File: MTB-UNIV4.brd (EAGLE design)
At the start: 100 x 80 mm, 91 parts, among them IC1 MEGA128-A, IC2 SN75176AP, IC3 NCP1117, IC4 ULN2803A, IC5 ULN2803A, X1 MKDSN1,5/4-5,08, X2 MKDSN1,5/4-5,08

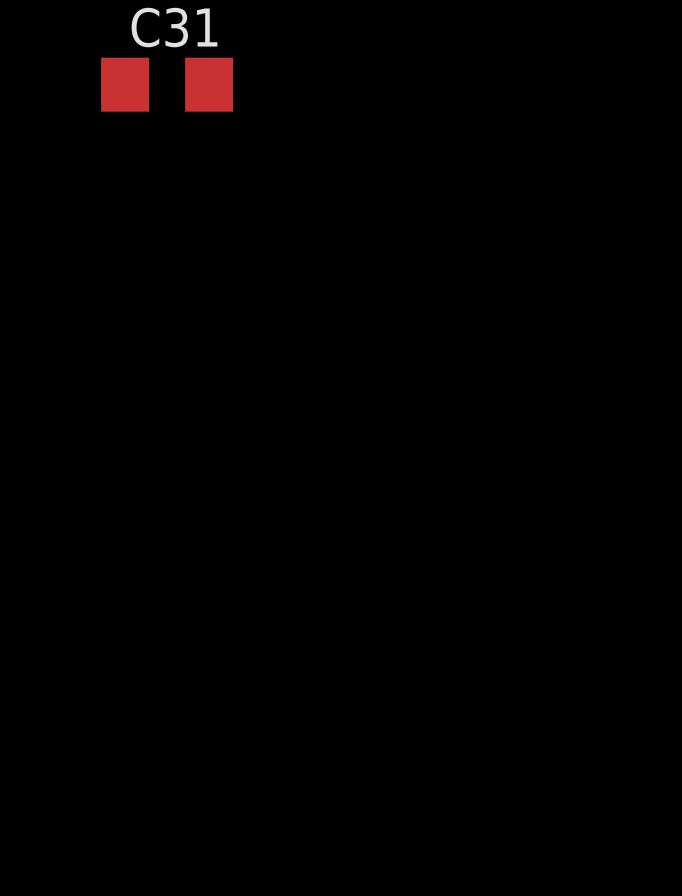
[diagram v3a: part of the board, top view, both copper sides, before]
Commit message: To stejné jako na vstupech ULN jsem udělal i na vstupu stabilizátoru. Tyristor v Crowbar obvodu proti přepětí.
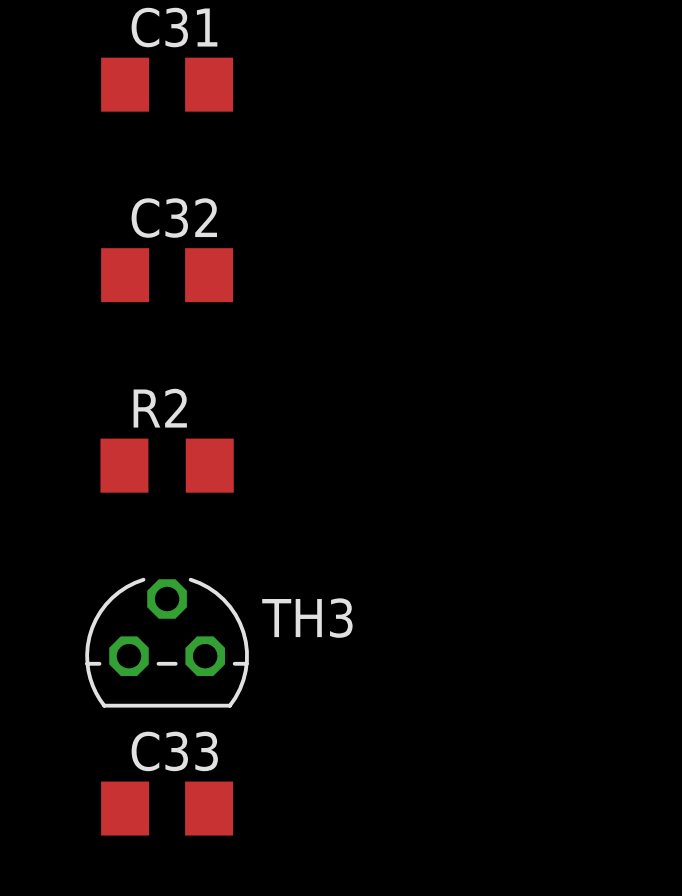
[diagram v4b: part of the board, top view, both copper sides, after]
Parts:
- added C32, C33: 100nF, rcl:C1206
- added R2: 2k2, rcl:R1206
- added TH3: MCR100, ElectroKrt:TO92
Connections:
- removed net N$14: D1.A, D2.C, F1.2
- new net N$57: C33.1, D2.A, R2.2, TH3.2
- new net N$58: C32.1, D1.A, F1.2
- net GND: now also C32.2, C33.2, R2.1, TH3.1; no longer D2.A
- net N$13: now also D2.C, TH3.3
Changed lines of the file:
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@@
 <attribute name="VALUE" x="-74.93" y="-614.68" size="1.27" layer="27"/>
+</element>
+<element name="C32" library="rcl" library_urn="urn:adsk.eagle:library:334" package="C1206" package3d_urn="urn:adsk.eagle:package:23618/2" value="100nF" x="-73.66" y="-618.49" smashed="yes">
+<attribute name="NAME" x="-74.93" y="-617.22" size="1.27" layer="25"/>
+<attribute name="POPULARITY" value="54" x="-73.66" y="-618.49" size="1.778" layer="27" display="off"/>
+<attribute name="SPICEPREFIX" value="C" x="-73.66" y="-618.49" size="1.778" layer="27" display="off"/>
+<attribute name="VALUE" x="-74.93" y="-621.03" size="1.27" layer="27"/>
+</element>
+<element name="R2" library="rcl" library_urn="urn:adsk.eagle:library:334" package="R1206" package3d_urn="urn:adsk.eagle:package:23540/2" value="2k2" x="-73.66" y="-624.84" smashed="yes">
+<attribute name="NAME" x="-74.93" y="-623.57" size="1.27" layer="25"/>
+<attribute name="POPULARITY" value="41" x="-73.66" y="-624.84" size="1.778" layer="27" display="off"/>
+<attribute name="SPICEPREFIX" value="R" x="-73.66" y="-624.84" size="1.778" layer="27" display="off"/>
+<attribute name="VALUE" x="-74.93" y="-627.38" size="1.27" layer="27"/>
+</element>
+<element name="TH3" library="ElectroKrt" package="TO92" package3d_urn="urn:adsk.eagle:package:28523/2" value="MCR100" x="-73.66" y="-631.19" smashed="yes">
+<attribute name="NAME" x="-70.485" y="-630.555" size="1.27" layer="25" ratio="10"/>
+<attribute name="PACKAGE" value="TO-92" x="-73.66" y="-631.19" size="1.778" layer="27" display="off"/>
+<attribute name="VALUE" x="-70.485" y="-632.46" size="1.27" layer="27" ratio="10"/>
+</element>
+<element name="C33" library="rcl" library_urn="urn:adsk.eagle:library:334" package="C1206" package3d_urn="urn:adsk.eagle:package:23618/2" value="100nF" x="-73.66" y="-636.27" smashed="yes">
+<attribute name="NAME" x="-74.93" y="-635" size="1.27" layer="25"/>
+<attribute name="POPULARITY" value="54" x="-73.66" y="-636.27" size="1.778" layer="27" display="off"/>
+<attribute name="SPICEPREFIX" value="C" x="-73.66" y="-636.27" size="1.778" layer="27" display="off"/>
+<attribute name="VALUE" x="-74.93" y="-638.81" size="1.27" layer="27"/>
 </element>
 </elements>
@@
 <contactref element="C8" pad="2"/>
 <contactref element="IC3" pad="1"/>
-<contactref element="D2" pad="A"/>
 <contactref element="C3" pad="2"/>
 <contactref element="X1" pad="4"/>
@@
 <contactref element="C31" pad="2"/>
 <contactref element="TH2" pad="1"/>
+<contactref element="R2" pad="1"/>
+<contactref element="C32" pad="2"/>
+<contactref element="C33" pad="2"/>
+<contactref element="TH3" pad="1"/>
 <wire x1="-64.77" y1="-439.42" x2="-67.31" y2="-439.42" width="0" layer="19" extent="1-1"/>
 <wire x1="-62.23" y1="-439.42" x2="-64.77" y2="-439.42" width="0" layer="19" extent="1-1"/>
@@
 <wire x1="-72.26" y1="-605.79" x2="-72.39" y2="-549.91" width="0" layer="19" extent="1-1"/>
 <wire x1="-72.26" y1="-612.14" x2="-72.26" y2="-605.79" width="0" layer="19" extent="1-1"/>
+<wire x1="-72.26" y1="-618.49" x2="-72.26" y2="-612.14" width="0" layer="19" extent="1-1"/>
+<wire x1="-75.082" y1="-624.84" x2="-72.26" y2="-618.49" width="0" layer="19" extent="1-1"/>
+<wire x1="-72.39" y1="-631.19" x2="-75.082" y2="-624.84" width="0" layer="19" extent="1-1"/>
+<wire x1="-72.26" y1="-636.27" x2="-72.39" y2="-631.19" width="0" layer="19" extent="1-1"/>
 <wire x1="-72.26" y1="-199.39" x2="-72.26" y2="-325.12" width="0" layer="19" extent="1-1"/>
 <wire x1="-69.24" y1="-191.77" x2="-72.26" y2="-199.39" width="0" layer="19" extent="1-1"/>
@@
 <wire x1="13.97" y1="-17.78" x2="-16.25" y2="-13.79" width="0" layer="19" extent="1-1"/>
 <wire x1="13.97" y1="-29.21" x2="13.97" y2="-17.78" width="0" layer="19" extent="1-1"/>
-<wire x1="0" y1="-146.05" x2="-31.62" y2="-107.95" width="0" layer="19" extent="1-1"/>
 </signal>
 <signal name="+5V">
@@
 <contactref element="C7" pad="1"/>
 <contactref element="IC3" pad="3"/>
+<contactref element="C25" pad="+"/>
+<contactref element="D2" pad="C"/>
+<contactref element="TH3" pad="3"/>
 <contactref element="D1" pad="C"/>
-<contactref element="C25" pad="+"/>
+<wire x1="-75.54" y1="-191.77" x2="-74.93" y2="-631.19" width="0" layer="19" extent="1-1"/>
+<wire x1="-68.71" y1="-120.65" x2="-75.54" y2="-191.77" width="0" layer="19" extent="1-1"/>
 <wire x1="-65.01" y1="-114.91" x2="-68.71" y2="-120.65" width="0" layer="19" extent="1-1"/>
-<wire x1="-75.54" y1="-191.77" x2="-68.71" y2="-120.65" width="0" layer="19" extent="1-1"/>
-<wire x1="-4.699" y1="-158.75" x2="-68.71" y2="-120.65" width="0" layer="19" extent="1-1"/>
-</signal>
-<signal name="N$14">
-<contactref element="D1" pad="A"/>
-<contactref element="D2" pad="C"/>
-<contactref element="F1" pad="2"/>
-<wire x1="-3.7" y1="-146.05" x2="-65.264" y2="-163.83" width="0" layer="19" extent="1-1"/>
-<wire x1="0" y1="-158.75" x2="-3.7" y2="-146.05" width="0" layer="19" extent="1-1"/>
+<wire x1="-3.7" y1="-146.05" x2="-65.01" y2="-114.91" width="0" layer="19" extent="1-1"/>
+<wire x1="-4.699" y1="-158.75" x2="-3.7" y2="-146.05" width="0" layer="19" extent="1-1"/>
 </signal>
 <signal name="V+">
@@
 <wire x1="-75.88" y1="-515.45" x2="-72.238" y2="-519.43" width="0" layer="19" extent="1-1"/>
 </signal>
+<signal name="N$57">
+<contactref element="R2" pad="2"/>
+<contactref element="D2" pad="A"/>
+<contactref element="C33" pad="1"/>
+<contactref element="TH3" pad="2"/>
+<wire x1="-73.66" y1="-629.285" x2="-75.06" y2="-636.27" width="0" layer="19" extent="1-1"/>
+<wire x1="-72.238" y1="-624.84" x2="-73.66" y2="-629.285" width="0" layer="19" extent="1-1"/>
+<wire x1="0" y1="-146.05" x2="-72.238" y2="-624.84" width="0" layer="19" extent="1-1"/>
+</signal>
+<signal name="N$58">
+<contactref element="F1" pad="2"/>
+<contactref element="C32" pad="1"/>
+<contactref element="D1" pad="A"/>
+<wire x1="0" y1="-158.75" x2="-65.264" y2="-163.83" width="0" layer="19" extent="1-1"/>
+<wire x1="-75.06" y1="-618.49" x2="-65.264" y2="-163.83" width="0" layer="19" extent="1-1"/>
+</signal>
 </signals>

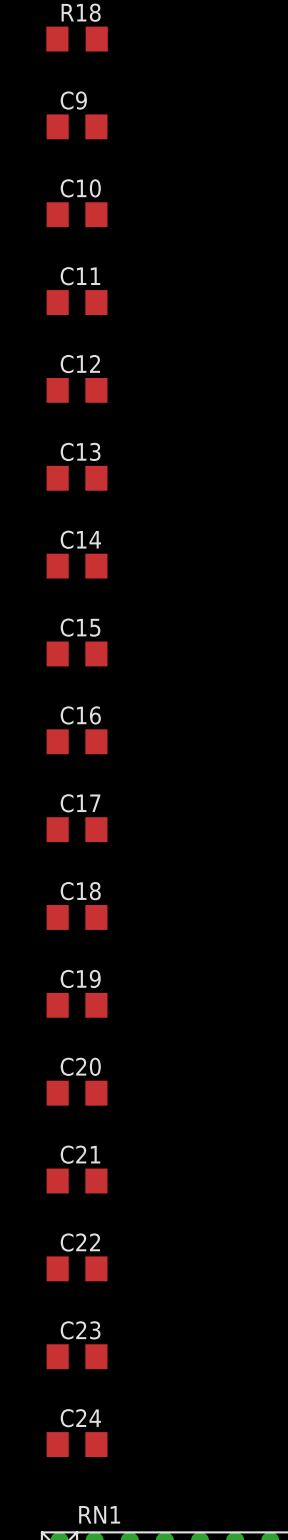
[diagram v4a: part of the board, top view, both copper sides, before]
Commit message: Odstraněny kondenzátory na vstupech
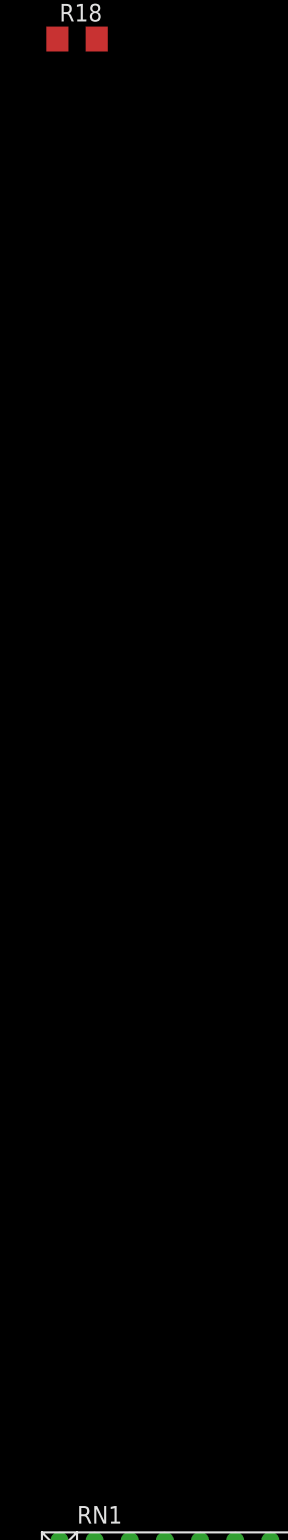
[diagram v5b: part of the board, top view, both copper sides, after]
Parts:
- removed C10, C11, C12, C13, C14, C15, C16, C17, C18, C19, C20, C21, C22, C23, C24, C9: 100nF, rcl:C1206
- IC2: value SN75176AP -> SN75176BP
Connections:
- net GND: no longer C10.2, C11.2, C12.2, C13.2, C14.2, C15.2, C16.2, C17.2, C18.2, C19.2, C20.2, C21.2, C22.2, C23.2, C24.2, C9.2
- net N$21: no longer C17.1
- net N$22: no longer C18.1
- net N$23: no longer C19.1
- net N$24: no longer C20.1
- net N$25: no longer C21.1
- net N$26: no longer C22.1
- net N$27: no longer C23.1
- net N$28: no longer C24.1
- net N$29: no longer C9.1
- net N$30: no longer C10.1
- net N$31: no longer C11.1
- net N$32: no longer C12.1
- net N$33: no longer C13.1
- net N$34: no longer C14.1
- net N$35: no longer C15.1
- net N$36: no longer C16.1

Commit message: Upraveno po změnách součástek z TME na GME, doplněny LED diody, nahrazeny headry na 9PIN (IO 8+1)
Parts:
- removed ISP1: AVRISP-6, adafruit:AVRISP
- added JP6: (no value), SparkFun-Connectors:2X8
- added LED1, LED2: (no value), adafruit:CHIPLED_1206
- added R21: 150R, rcl:R1206
- added R22: 91R, rcl:R1206
- D2: value Zener -> (none); device adafruit:SOD-123 -> diode:SOT23
- F1: device adafruit:1812 -> ElectroKrt:1X2-BIGPOGO-5MM
- IC3: value NCP1117 -> MC7805CDTG; device ElectroKrt:SOT223 -> LDO:MC78M05BDTRKG
- JP1: value (none) -> AVRISP-6; device adafruit:1X08-BIG -> adafruit:AVRISP
- JP2, JP3, JP4: device adafruit:1X08-BIG -> adafruit:1X09-BIG
- JP5: device SparkFun-Connectors:2X8 -> adafruit:1X09-BIG
- X1, X2: value MKDSN1,5/4-5,08 -> CON-04-5.0CON-5MM; device con-phoenix-508:MKDSN1,5/4-5,08 -> ElectroKrt:MKDSN1,5/4-5,00
- moved X2 581.8 mm to (-7.50, -661.6)
- moved X1 580.6 mm to (-7.50, -648.9)
- moved IC3 569.2 mm to (-83.8, -680.7)
- moved JP2 561.0 mm to (-10.2, -739.1)
- moved D2 529.6 mm to (-74.9, -670.6)
- moved F1 527.3 mm to (0.00, -686.9)
- moved JP4 517.4 mm to (-10.2, -726.4)
- moved JP3 509.8 mm to (-10.2, -713.7)
- moved JP5 316.6 mm to (-10.2, -751.8)
- moved JP1 62.3 mm to (-57.1, -113.0)
- renumbered C25 to C10, C26 to C11, C27 to C9, C28 to C14, C29 to C15, C30 to C16, C31 to C17, C32 to C12, C33 to C13
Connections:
- new net N$14: IC1.16, R22.2
- new net N$59: IC1.17, R21.2
- new net N$60: LED2.A, R21.1
- new net N$61: LED1.A, R22.1
- net +5V: now also IC3.3, JP1.2; no longer IC3.2, IC3.4, ISP1.2
- net ADDR-1: now also JP6.1; no longer JP5.1
- net ADDR-2: now also JP6.3; no longer JP5.3
- net ADDR-3: now also JP6.5; no longer JP5.5
- net ADDR-4: now also JP6.7; no longer JP5.7
- net ADDR-5: now also JP6.9; no longer JP5.9
- net ADDR-6: now also JP6.11; no longer JP5.11
- net ADDR-7: now also JP6.13; no longer JP5.13
- net ADDR-8: now also JP6.15; no longer JP5.15
- net GND: now also IC3.2, JP1.6, JP2.9, JP3.9, JP4.9, JP5.9, JP6.10, JP6.12, JP6.14, JP6.16, JP6.2, JP6.4, JP6.6, JP6.8, LED1.C, LED2.C; no longer IC3.1, ISP1.6, JP5.10, JP5.12, JP5.14, JP5.16, JP5.2, JP5.4, JP5.6, JP5.8
- net MISO: now also JP1.1; no longer ISP1.1
- net MOSI: now also JP1.4; no longer ISP1.4
- net N$10: now also JP2.8; no longer JP1.8
- net N$12: now also JP3.1; no longer JP2.1
- net N$13: now also D2.3, IC3.1; no longer D2.C, IC3.3
- net N$15: now also JP3.2; no longer JP2.2
- net N$16: now also JP3.3; no longer JP2.3
- net N$17: now also JP3.4; no longer JP2.4
- net N$18: now also JP3.5; no longer JP2.5
- net N$19: now also JP3.6; no longer JP2.6
- net N$2: now also JP2.1; no longer JP1.1
- net N$20: now also JP3.7; no longer JP2.7
- net N$21: now also JP5.1; no longer JP4.1
- net N$22: now also JP5.2; no longer JP4.2
- net N$23: now also JP5.3; no longer JP4.3
- net N$24: now also JP5.4; no longer JP4.4
- net N$25: now also JP5.5; no longer JP4.5
- net N$26: now also JP5.6; no longer JP4.6
- net N$27: now also JP5.7; no longer JP4.7
- net N$28: now also JP5.8; no longer JP4.8
- net N$29: now also JP4.1; no longer JP3.1
- net N$30: now also JP4.2; no longer JP3.2
- net N$31: now also JP4.3; no longer JP3.3
- net N$32: now also JP4.4; no longer JP3.4
- net N$33: now also JP4.5; no longer JP3.5
- net N$34: now also JP4.6; no longer JP3.6
- net N$35: now also JP4.7; no longer JP3.7
- net N$36: now also JP4.8; no longer JP3.8
- net N$4: now also JP2.2; no longer JP1.2
- net N$47: now also JP3.8; no longer JP2.8
- net N$5: now also JP2.3; no longer JP1.3
- net N$57: now also D2.1; no longer D2.A
- net N$58: now also F1.P$2; no longer F1.2
- net N$6: now also JP2.4; no longer JP1.4
- net N$7: now also JP2.5; no longer JP1.5
- net N$8: now also JP2.6; no longer JP1.6
- net N$9: now also JP2.7; no longer JP1.7
- net RST: now also JP1.5; no longer ISP1.5
- net SCK: now also JP1.3; no longer ISP1.3
- net V+: now also F1.P$1; no longer F1.1

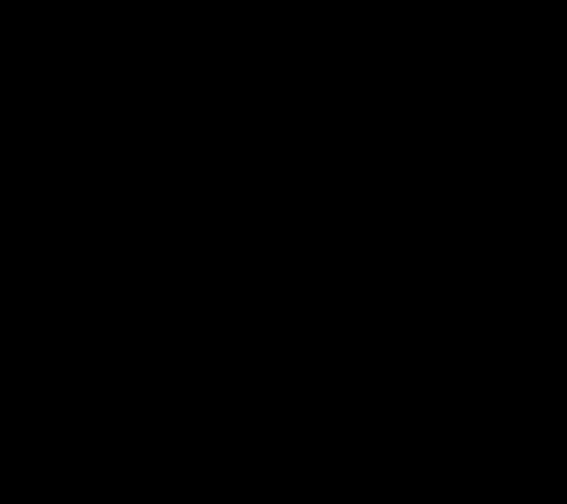
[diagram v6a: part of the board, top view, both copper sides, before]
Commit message: přidány vodící prvky pro Pick&Place stroje
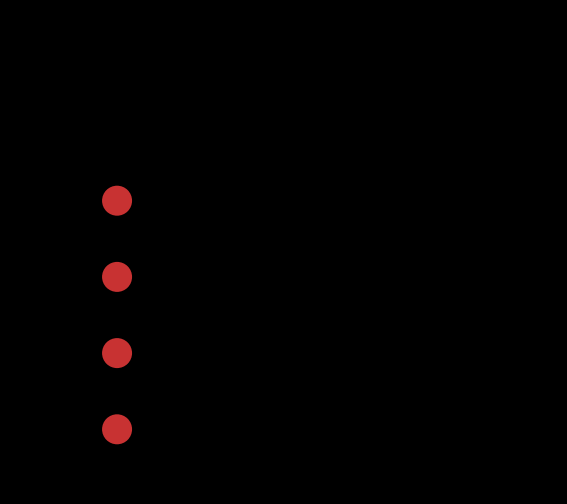
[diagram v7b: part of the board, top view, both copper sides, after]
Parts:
- added U$1, U$2, U$3, U$4: FIDUCIAL, adafruit:FIDUCIAL_1MM
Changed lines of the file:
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@@
 <attribute name="VALUE" x="-99.06" y="-703.58" size="1.27" layer="27"/>
 </element>
+<element name="U$1" library="adafruit" library_urn="urn:adsk.eagle:library:420" package="FIDUCIAL_1MM" package3d_urn="urn:adsk.eagle:package:6240632/1" value="FIDUCIAL" x="-99.06" y="-754.38" smashed="yes"/>
+<element name="U$2" library="adafruit" library_urn="urn:adsk.eagle:library:420" package="FIDUCIAL_1MM" package3d_urn="urn:adsk.eagle:package:6240632/1" value="FIDUCIAL" x="-99.06" y="-756.92" smashed="yes"/>
+<element name="U$3" library="adafruit" library_urn="urn:adsk.eagle:library:420" package="FIDUCIAL_1MM" package3d_urn="urn:adsk.eagle:package:6240632/1" value="FIDUCIAL" x="-99.06" y="-759.46" smashed="yes"/>
+<element name="U$4" library="adafruit" library_urn="urn:adsk.eagle:library:420" package="FIDUCIAL_1MM" package3d_urn="urn:adsk.eagle:package:6240632/1" value="FIDUCIAL" x="-99.06" y="-762" smashed="yes"/>
 </elements>
 <signals>

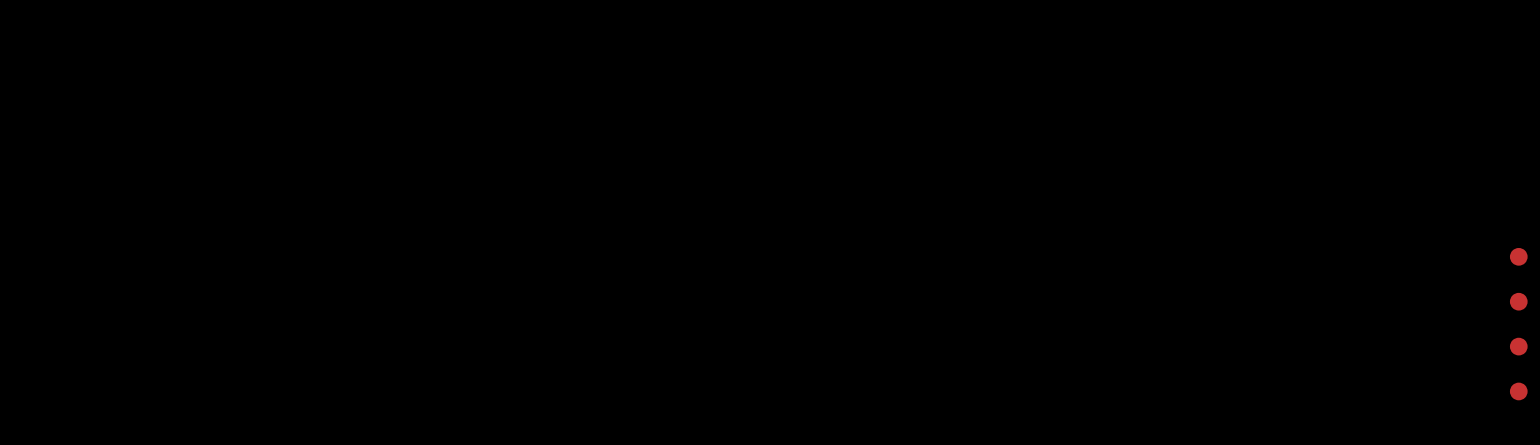
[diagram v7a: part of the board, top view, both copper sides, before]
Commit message: Přidán na test molex 3-pin 8x pro jeden výstup.
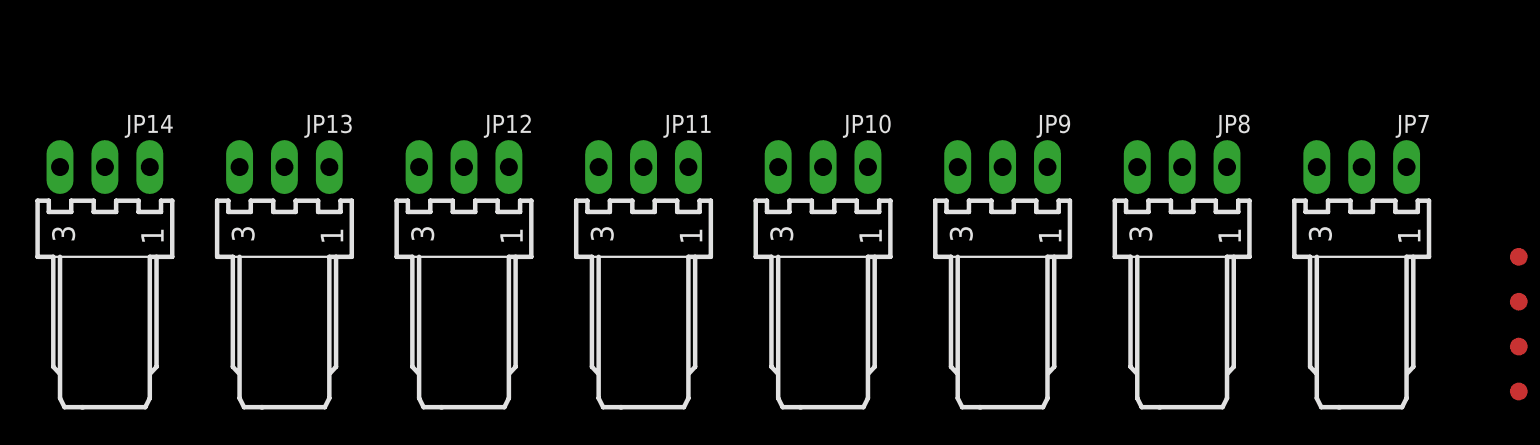
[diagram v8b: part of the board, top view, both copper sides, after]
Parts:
- added JP10, JP11, JP12, JP13, JP14, JP7, JP8, JP9: 22-05-7038-03, con-molex:7395-03
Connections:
- net GND: now also JP10.3, JP11.3, JP12.3, JP13.3, JP14.3, JP7.3, JP8.3, JP9.3
- net N$10: now also JP14.2
- net N$2: now also JP7.2
- net N$4: now also JP8.2
- net N$5: now also JP9.2
- net N$6: now also JP10.2
- net N$7: now also JP11.2
- net N$8: now also JP12.2
- net N$9: now also JP13.2
